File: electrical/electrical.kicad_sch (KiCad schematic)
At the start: 0 parts

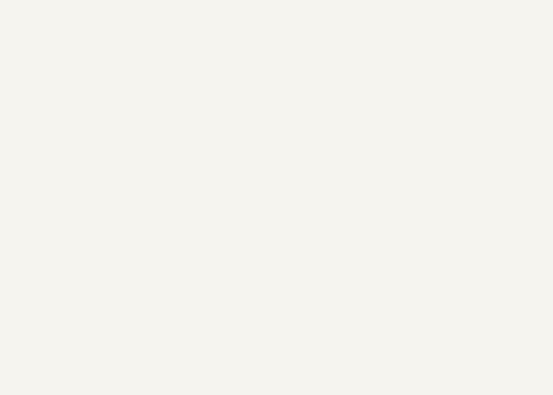
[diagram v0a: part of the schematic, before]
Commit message: Added overview placeholder and renumbered other pages.
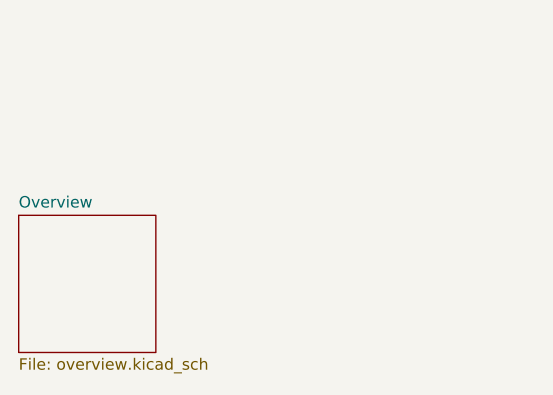
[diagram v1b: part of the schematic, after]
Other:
- added sheet Overview (overview.kicad_sch)

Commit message: Updated system overview and added Power 2 to GTX 45R.
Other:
- sheet Power ports: added GTX45R_BAK_PWR; removed none
- sheet Transponder ports: added GTX45R_BAK_PWR; removed none

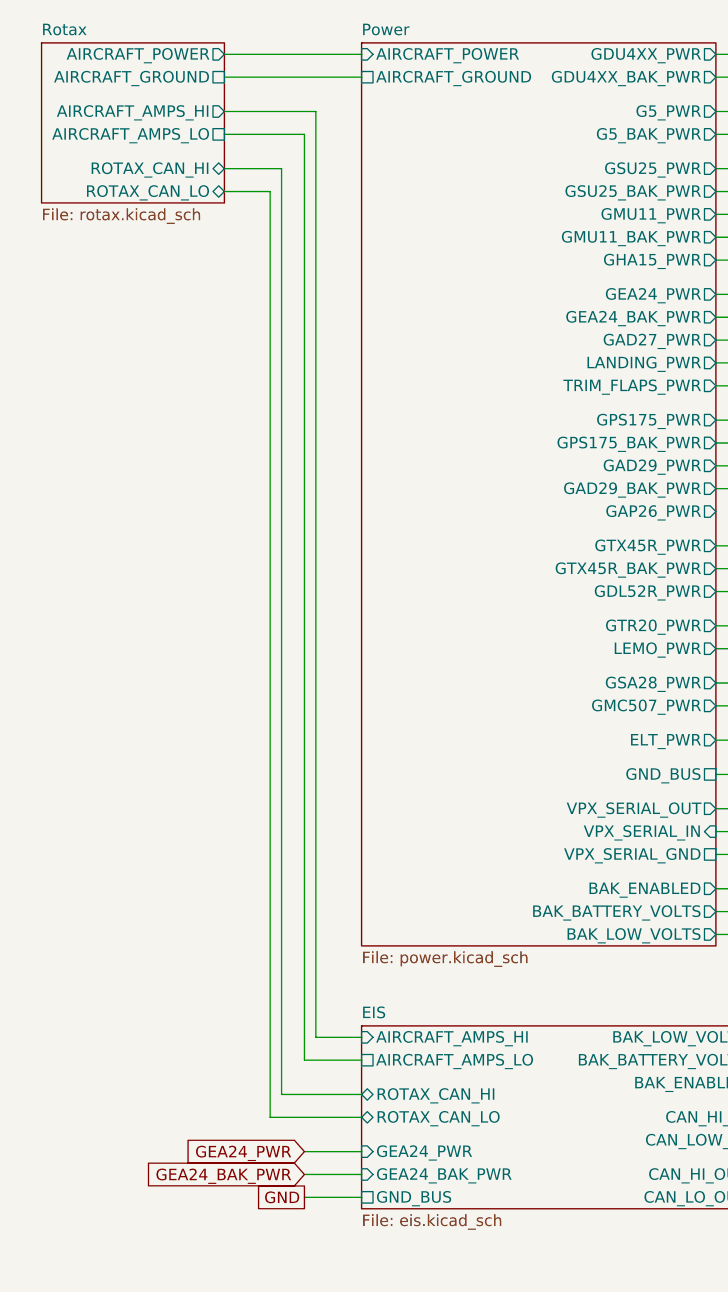
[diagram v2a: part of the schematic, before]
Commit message: Removed Amps as Rotax sends that over Can to GEA24
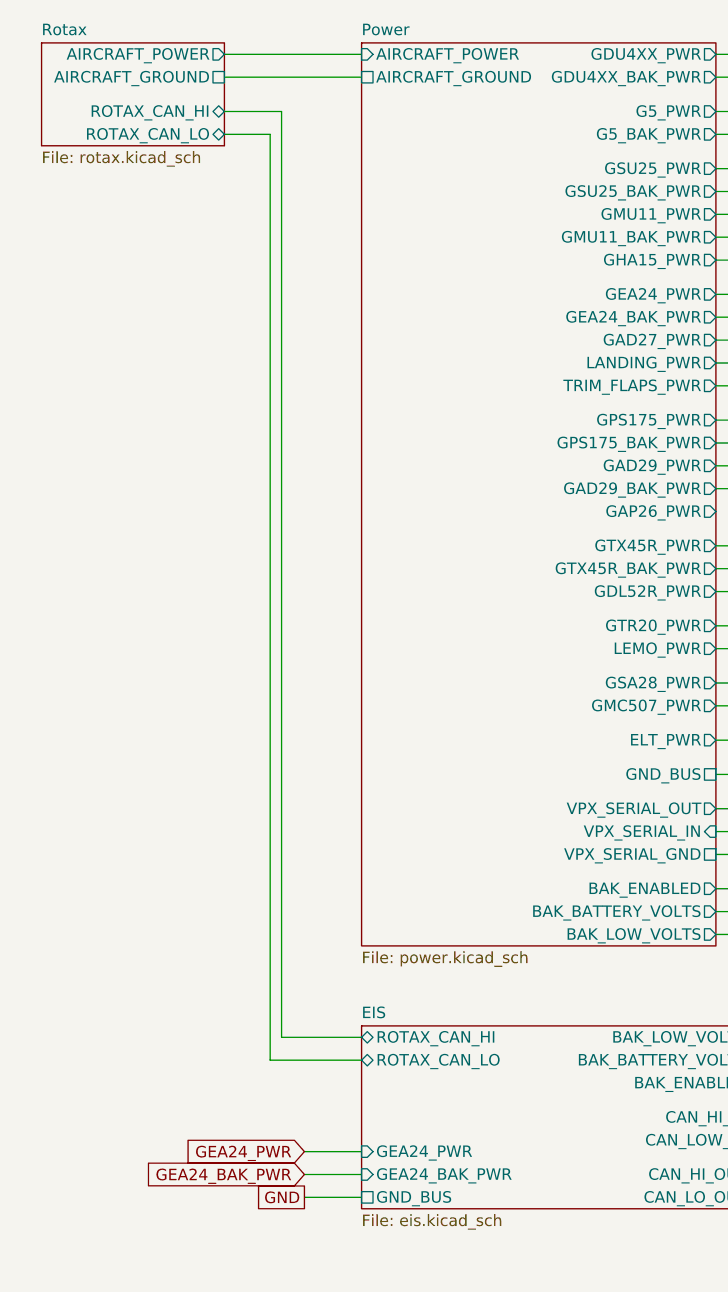
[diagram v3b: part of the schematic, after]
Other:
- sheet EIS ports: added none; removed AIRCRAFT_AMPS_HI, AIRCRAFT_AMPS_LO
- sheet Rotax ports: added none; removed AIRCRAFT_AMPS_HI, AIRCRAFT_AMPS_LO
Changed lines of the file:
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@@
     (stroke (width 0) (type default))
   )
-  (wire (pts (xy 44.45 146.05) (xy 53.34 146.05))
+  (wire (pts (xy 44.45 139.7) (xy 53.34 139.7))
     (stroke (width 0) (type default))
   )
@@
     (stroke (width 0) (type default))
   )
-  (wire (pts (xy 43.18 148.59) (xy 53.34 148.59))
+  (wire (pts (xy 43.18 142.24) (xy 53.34 142.24))
     (stroke (width 0) (type default))
   )
@@
     (stroke (width 0) (type default))
   )
-  (wire (pts (xy 38.1 39.37) (xy 46.99 39.37))
-    (stroke (width 0) (type default))
-  )
   (wire (pts (xy 102.87 125.73) (xy 102.87 142.24))
     (stroke (width 0) (type default))
@@
     (stroke (width 0) (type default))
   )
-  (wire (pts (xy 48.26 36.83) (xy 48.26 139.7))
-    (stroke (width 0) (type default))
-  )
   (wire (pts (xy 92.71 78.74) (xy 96.52 78.74))
     (stroke (width 0) (type default))
@@
     (stroke (width 0) (type default))
   )
-  (wire (pts (xy 38.1 43.18) (xy 44.45 43.18))
+  (wire (pts (xy 38.1 36.83) (xy 44.45 36.83))
     (stroke (width 0) (type default))
   )
@@
     (stroke (width 0) (type default))
   )
-  (wire (pts (xy 46.99 39.37) (xy 46.99 142.24))
-    (stroke (width 0) (type default))
-  )
   (wire (pts (xy 257.81 107.95) (xy 257.81 173.99))
     (stroke (width 0) (type default))
@@
     (stroke (width 0) (type default))
   )
-  (wire (pts (xy 44.45 43.18) (xy 44.45 146.05))
+  (wire (pts (xy 44.45 36.83) (xy 44.45 139.7))
     (stroke (width 0) (type default))
   )
@@
     (stroke (width 0) (type default))
   )
-  (wire (pts (xy 43.18 45.72) (xy 43.18 148.59))
+  (wire (pts (xy 43.18 39.37) (xy 43.18 142.24))
     (stroke (width 0) (type default))
   )
@@
     (stroke (width 0) (type default))
   )
-  (wire (pts (xy 38.1 45.72) (xy 43.18 45.72))
+  (wire (pts (xy 38.1 39.37) (xy 43.18 39.37))
     (stroke (width 0) (type default))
   )
@@
     (stroke (width 0) (type default))
   )
-  (wire (pts (xy 38.1 36.83) (xy 48.26 36.83))
-    (stroke (width 0) (type default))
-  )
   (wire (pts (xy 92.71 90.17) (xy 173.99 90.17))
     (stroke (width 0) (type default))
@@
     (stroke (width 0) (type default))
   )
-  (wire (pts (xy 46.99 142.24) (xy 53.34 142.24))
-    (stroke (width 0) (type default))
-  )
   (wire (pts (xy 92.71 128.27) (xy 101.6 128.27))
     (stroke (width 0) (type default))
@@
   )
   (wire (pts (xy 46.99 152.4) (xy 53.34 152.4))
-    (stroke (width 0) (type default))
-  )
-  (wire (pts (xy 48.26 139.7) (xy 53.34 139.7))
     (stroke (width 0) (type default))
   )
@@
     )
   )
-  (sheet (at 17.78 29.21) (size 20.32 17.78) (fields_autoplaced)
+  (sheet (at 17.78 29.21) (size 20.32 11.43) (fields_autoplaced)
     (stroke (width 0.1524) (type solid))
     (fill (color 0 0 0 0.0000))
@@
       (effects (font (size 1.27 1.27)) (justify left bottom))
     )
-    (property "Sheetfile" "rotax.kicad_sch" (at 17.78 47.5746 0)
+    (property "Sheetfile" "rotax.kicad_sch" (at 17.78 41.2246 0)
       (effects (font (size 1.27 1.27)) (justify left top))
     )
@@
       (effects (font (size 1.27 1.27)) (justify right))
     )
-    (pin "AIRCRAFT_AMPS_HI" output (at 38.1 36.83 0)
-      (effects (font (size 1.27 1.27)) (justify right))
-    )
-    (pin "AIRCRAFT_AMPS_LO" passive (at 38.1 39.37 0)
-      (effects (font (size 1.27 1.27)) (justify right))
-    )
-    (pin "ROTAX_CAN_LO" bidirectional (at 38.1 45.72 0)
-      (effects (font (size 1.27 1.27)) (justify right))
-    )
-    (pin "ROTAX_CAN_HI" bidirectional (at 38.1 43.18 0)
+    (pin "ROTAX_CAN_LO" bidirectional (at 38.1 39.37 0)
+      (effects (font (size 1.27 1.27)) (justify right))
+    )
+    (pin "ROTAX_CAN_HI" bidirectional (at 38.1 36.83 0)
       (effects (font (size 1.27 1.27)) (justify right))
     )
@@
       (effects (font (size 1.27 1.27)) (justify left))
     )
-    (pin "ROTAX_CAN_HI" bidirectional (at 53.34 146.05 180)
-      (effects (font (size 1.27 1.27)) (justify left))
-    )
-    (pin "ROTAX_CAN_LO" bidirectional (at 53.34 148.59 180)
+    (pin "ROTAX_CAN_HI" bidirectional (at 53.34 139.7 180)
+      (effects (font (size 1.27 1.27)) (justify left))
+    )
+    (pin "ROTAX_CAN_LO" bidirectional (at 53.34 142.24 180)
       (effects (font (size 1.27 1.27)) (justify left))
     )
@@
       (effects (font (size 1.27 1.27)) (justify right))
     )
-    (pin "AIRCRAFT_AMPS_HI" input (at 53.34 139.7 180)
-      (effects (font (size 1.27 1.27)) (justify left))
-    )
-    (pin "AIRCRAFT_AMPS_LO" passive (at 53.34 142.24 180)
-      (effects (font (size 1.27 1.27)) (justify left))
-    )
     (pin "BAK_ENABLED" input (at 97.79 144.78 0)

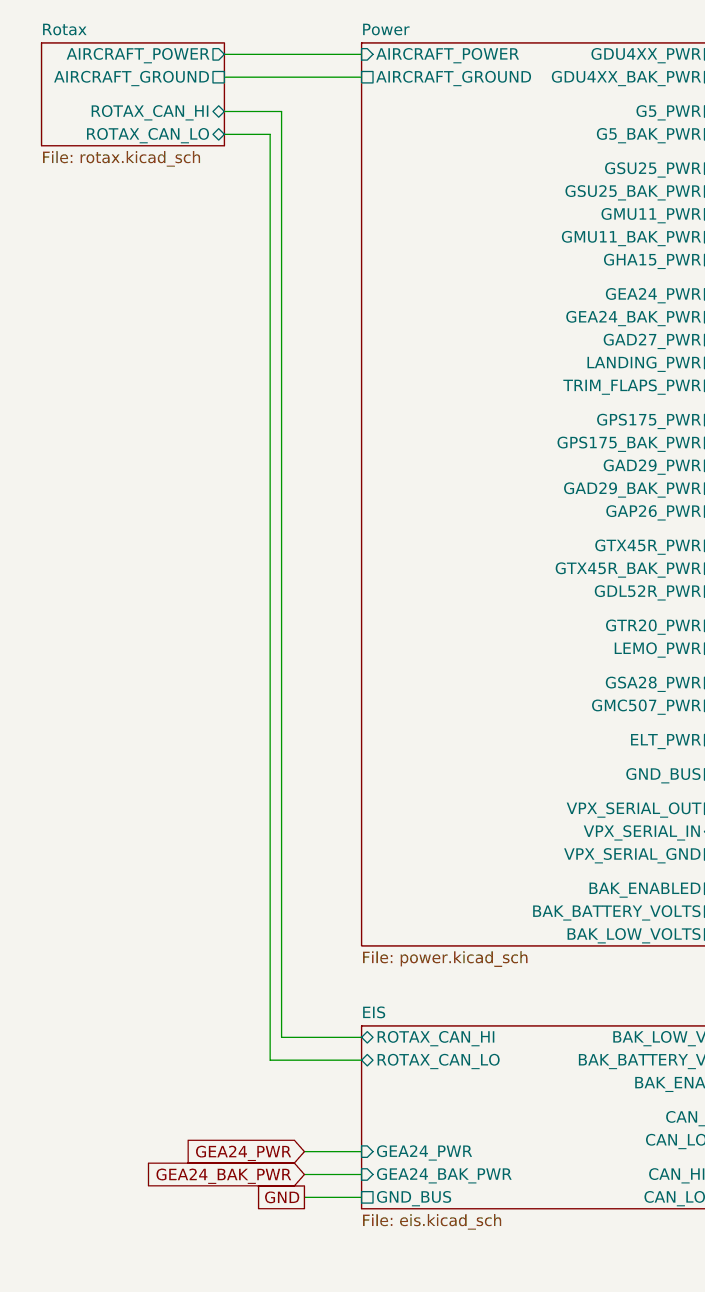
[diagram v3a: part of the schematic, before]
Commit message: Changed Rotax Canbus to be 2 connections
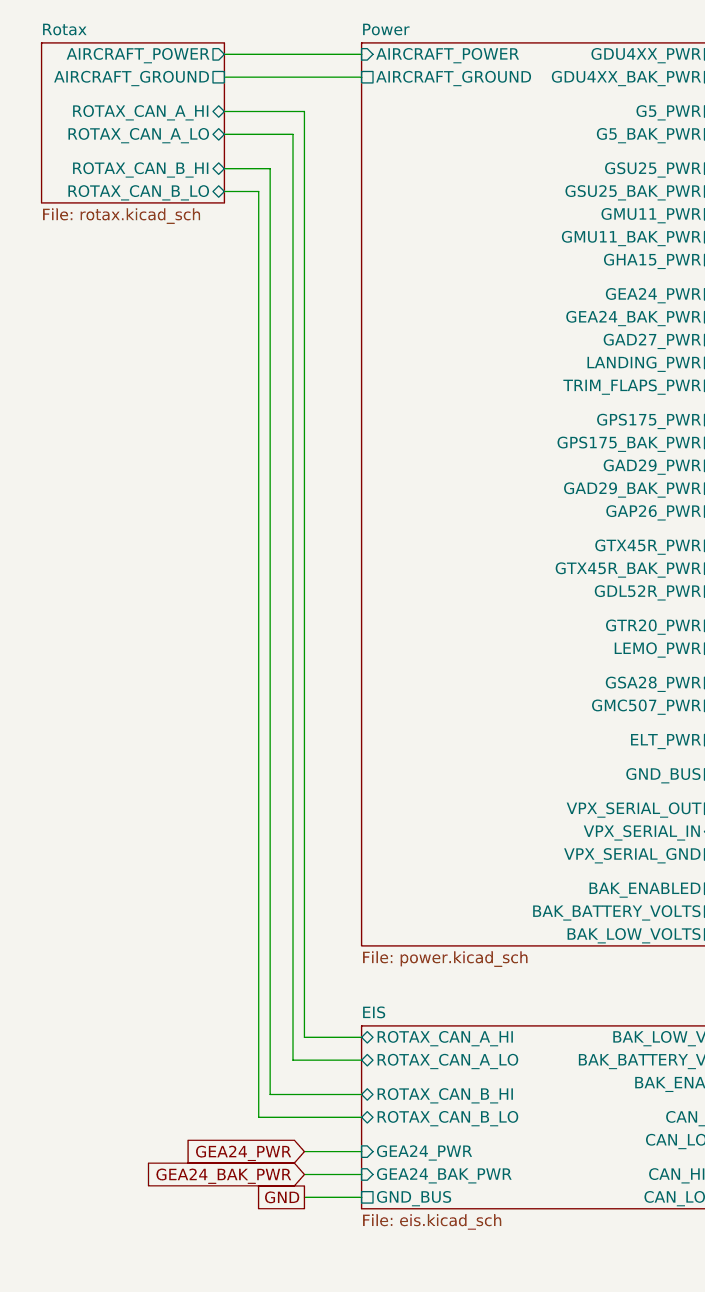
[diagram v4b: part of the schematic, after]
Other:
- sheet EIS ports: added ROTAX_CAN_A_HI, ROTAX_CAN_A_LO, ROTAX_CAN_B_HI, ROTAX_CAN_B_LO; removed ROTAX_CAN_HI, ROTAX_CAN_LO
- sheet Rotax ports: added ROTAX_CAN_A_HI, ROTAX_CAN_A_LO, ROTAX_CAN_B_HI, ROTAX_CAN_B_LO; removed ROTAX_CAN_HI, ROTAX_CAN_LO
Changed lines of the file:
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@@
     (stroke (width 0) (type default))
   )
-  (wire (pts (xy 44.45 139.7) (xy 53.34 139.7))
+  (wire (pts (xy 46.99 139.7) (xy 53.34 139.7))
     (stroke (width 0) (type default))
   )
@@
     (stroke (width 0) (type default))
   )
-  (wire (pts (xy 43.18 142.24) (xy 53.34 142.24))
+  (wire (pts (xy 45.72 142.24) (xy 53.34 142.24))
     (stroke (width 0) (type default))
   )
@@
     (stroke (width 0) (type default))
   )
+  (wire (pts (xy 53.34 148.59) (xy 41.91 148.59))
+    (stroke (width 0) (type default))
+  )
   (wire (pts (xy 356.87 66.04) (xy 365.76 66.04))
     (stroke (width 0) (type default))
@@
     (stroke (width 0) (type default))
   )
-  (wire (pts (xy 38.1 36.83) (xy 44.45 36.83))
-    (stroke (width 0) (type default))
-  )
   (wire (pts (xy 220.98 77.47) (xy 309.88 77.47))
     (stroke (width 0) (type default))
@@
     (stroke (width 0) (type default))
   )
+  (wire (pts (xy 43.18 146.05) (xy 53.34 146.05))
+    (stroke (width 0) (type default))
+  )
   (wire (pts (xy 158.75 207.01) (xy 312.42 207.01))
     (stroke (width 0) (type default))
@@
     (stroke (width 0) (type default))
   )
+  (wire (pts (xy 43.18 43.18) (xy 43.18 146.05))
+    (stroke (width 0) (type default))
+  )
   (wire (pts (xy 356.87 74.93) (xy 365.76 74.93))
     (stroke (width 0) (type default))
@@
     (stroke (width 0) (type default))
   )
+  (wire (pts (xy 41.91 45.72) (xy 38.1 45.72))
+    (stroke (width 0) (type default))
+  )
   (wire (pts (xy 97.79 154.94) (xy 109.22 154.94))
     (stroke (width 0) (type default))
@@
     (stroke (width 0) (type default))
   )
+  (wire (pts (xy 38.1 43.18) (xy 43.18 43.18))
+    (stroke (width 0) (type default))
+  )
   (wire (pts (xy 356.87 68.58) (xy 365.76 68.58))
     (stroke (width 0) (type default))
@@
     (stroke (width 0) (type default))
   )
-  (wire (pts (xy 44.45 36.83) (xy 44.45 139.7))
+  (wire (pts (xy 46.99 36.83) (xy 46.99 139.7))
     (stroke (width 0) (type default))
   )
@@
     (stroke (width 0) (type default))
   )
-  (wire (pts (xy 43.18 39.37) (xy 43.18 142.24))
+  (wire (pts (xy 38.1 39.37) (xy 45.72 39.37))
+    (stroke (width 0) (type default))
+  )
+  (wire (pts (xy 45.72 39.37) (xy 45.72 142.24))
     (stroke (width 0) (type default))
   )
@@
     (stroke (width 0) (type default))
   )
-  (wire (pts (xy 38.1 39.37) (xy 43.18 39.37))
-    (stroke (width 0) (type default))
-  )
   (wire (pts (xy 299.72 107.95) (xy 309.88 107.95))
     (stroke (width 0) (type default))
   )
+  (wire (pts (xy 41.91 148.59) (xy 41.91 45.72))
+    (stroke (width 0) (type default))
+  )
   (wire (pts (xy 303.53 53.34) (xy 303.53 68.58))
     (stroke (width 0) (type default))
@@
   )
   (wire (pts (xy 309.88 50.8) (xy 302.26 50.8))
+    (stroke (width 0) (type default))
+  )
+  (wire (pts (xy 38.1 36.83) (xy 46.99 36.83))
     (stroke (width 0) (type default))
   )
@@
     )
   )
-  (sheet (at 17.78 29.21) (size 20.32 11.43) (fields_autoplaced)
+  (sheet (at 17.78 29.21) (size 20.32 17.78) (fields_autoplaced)
     (stroke (width 0.1524) (type solid))
     (fill (color 0 0 0 0.0000))
@@
       (effects (font (size 1.27 1.27)) (justify left bottom))
     )
-    (property "Sheetfile" "rotax.kicad_sch" (at 17.78 41.2246 0)
+    (property "Sheetfile" "rotax.kicad_sch" (at 17.78 47.5746 0)
       (effects (font (size 1.27 1.27)) (justify left top))
     )
@@
       (effects (font (size 1.27 1.27)) (justify right))
     )
-    (pin "ROTAX_CAN_LO" bidirectional (at 38.1 39.37 0)
-      (effects (font (size 1.27 1.27)) (justify right))
-    )
-    (pin "ROTAX_CAN_HI" bidirectional (at 38.1 36.83 0)
+    (pin "ROTAX_CAN_A_LO" bidirectional (at 38.1 39.37 0)
+      (effects (font (size 1.27 1.27)) (justify right))
+    )
+    (pin "ROTAX_CAN_B_LO" bidirectional (at 38.1 45.72 0)
+      (effects (font (size 1.27 1.27)) (justify right))
+    )
+    (pin "ROTAX_CAN_B_HI" bidirectional (at 38.1 43.18 0)
+      (effects (font (size 1.27 1.27)) (justify right))
+    )
+    (pin "ROTAX_CAN_A_HI" bidirectional (at 38.1 36.83 0)
       (effects (font (size 1.27 1.27)) (justify right))
     )
@@
       (effects (font (size 1.27 1.27)) (justify left))
     )
-    (pin "ROTAX_CAN_HI" bidirectional (at 53.34 139.7 180)
-      (effects (font (size 1.27 1.27)) (justify left))
-    )
-    (pin "ROTAX_CAN_LO" bidirectional (at 53.34 142.24 180)
-      (effects (font (size 1.27 1.27)) (justify left))
-    )
     (pin "CAN_HI_OUT" bidirectional (at 97.79 154.94 0)
       (effects (font (size 1.27 1.27)) (justify right))
@@
       (effects (font (size 1.27 1.27)) (justify right))
     )
+    (pin "ROTAX_CAN_A_HI" bidirectional (at 53.34 139.7 180)
+      (effects (font (size 1.27 1.27)) (justify left))
+    )
+    (pin "ROTAX_CAN_A_LO" bidirectional (at 53.34 142.24 180)
+      (effects (font (size 1.27 1.27)) (justify left))
+    )
+    (pin "ROTAX_CAN_B_HI" bidirectional (at 53.34 146.05 180)
+      (effects (font (size 1.27 1.27)) (justify left))
+    )
+    (pin "ROTAX_CAN_B_LO" bidirectional (at 53.34 148.59 180)
+      (effects (font (size 1.27 1.27)) (justify left))
+    )
     (instances
